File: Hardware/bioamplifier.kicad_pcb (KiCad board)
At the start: 4 copper layers, 73.2 x 45 mm, 86 parts, among them IC1 MCP1754ST-3302E_DB, J1 Conn_01x07_Socket, J2 Conn_01x26_Pin, J3 Conn_01x07_Socket, U1 ADS1299IPAG, U10 TPD4E1B06DCKR, U11 LM2665M6, U12 TLV77333PDQNR, U2 TPD4E1B06DCKR, U3 TPD4E1B06DCKR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

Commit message: Fix Last DRC Errors
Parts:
- removed IC1: MCP1754ST-3302E_DB, mcp1754:SOT230P700X180-4N
- removed U12: TLV77333PDQNR, tlv77333:X2SON_DQN4_TEX
- moved C29 31.5 mm to (118.9, 108.5), turned to -90 degrees
- moved C41 29.3 mm to (116.9, 108.5), turned to -90 degrees
- moved C25 28.7 mm to (107.8, 108.7), turned to -90 degrees
- moved C40 27.8 mm to (100.0, 107.3), turned to 90 degrees
- moved U6 26.4 mm to (116.9, 104.5), turned to 0 degrees
- moved U8 26.1 mm to (104.5, 107.5), turned to 180 degrees
- moved C46 25.8 mm to (91.0, 108.1), turned to 0 degrees
- moved C27 20.2 mm to (112.9, 102.0)
- moved C45 18.9 mm to (86.9, 109.1), turned to -90 degrees
- moved U11 18.9 mm to (86.9, 109.1), turned to 0 degrees
- moved R8 15.2 mm to (102.2, 92.0), turned to 0 degrees
- moved J3 14.2 mm to (106.0, 79.3), turned to 0 degrees
- moved R7 11.7 mm to (102.2, 89.0), turned to 0 degrees
- moved R1 11.4 mm to (100.0, 90.8), turned to -90 degrees
- moved R6 9.82 mm to (102.3, 86.9), turned to 0 degrees
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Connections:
- C11 pad 1: AVSS -> GNDA
- C12 pad 1: AVSS -> GNDA
- C13 pad 1: AVSS -> GNDA
- C14 pad 1: AVSS -> GNDA
- C15 pad 1: AVSS -> GNDA
- C16 pad 1: AVSS -> GNDA
- C17 pad 1: AVSS -> GNDA
- C18 pad 1: AVSS -> GNDA
- C2 pad 1: /DVDD -> DVDD
- C25 pad 1: AVSS -> GNDA
- C26 pad 1: AVSS -> GNDA
- C28 pad 1: AVSS -> GNDA
- C3 pad 1: /DVDD -> DVDD
- C31 pad 1: AVSS -> GNDA
- C32 pad 1: AVSS -> GNDA
- C33 pad 1: AVSS -> GNDA
- C34 pad 1: AVSS -> GNDA
- C35 pad 1: AVSS -> GNDA
- C36 pad 1: AVSS -> GNDA
- C37 pad 2: AVSS -> GNDA
- C38 pad 1: AVSS -> GNDA
- C39 pad 1: AVSS -> GNDA
- C40 pad 2: AVSS -> GNDA
- C42 pad 2: AVSS -> GNDA
- C43 pad 2: AVSS -> GNDA
- C44 pad 2: AVSS -> GNDA
- C46 pad 2: AVSS -> GNDA
- J2 pad 1: AVSS -> GNDA
- J2 pad 2: AVSS -> GNDA
- JP2 pad 2: AVSS -> GNDA
- U1 pad 31: AVSS -> GNDA
- U1 pad 50: /DVDD -> DVDD
- U1 pad 60: AVSS -> GNDA
- U10 pad 3: AVSS -> GNDA
- U11 pad 2: AVSS -> GNDA
- U2 pad 3: AVSS -> GNDA
- U3 pad 3: AVSS -> GNDA
- U4 pad 3: AVSS -> GNDA
- U5 pad 3: AVSS -> GNDA
- U7 pad 1: AVSS -> GNDA
- U8 pad 2: AVSS -> GNDA
- U8 pad 4: AVSS -> GNDA
- U9 pad 3: AVSS -> GNDA
- U9 pad 4: AVSS -> GNDA
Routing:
- net AVSS: track 43.5 -> 93.0 mm, vias 6 -> 5
- net DVDD: track 38.4 -> 79.3 mm, vias 0 -> 5
- net GNDA: track 0.00 -> 33.5 mm, vias 0 -> 9
- net /DVDD: track 23.1 -> 0.00 mm, vias 1 -> 0
- net AVDD: track 47.9 -> 68.2 mm
- net GNDD: track 31.2 -> 44.9 mm
- net (no net): track 11.4 -> 0.00 mm
- net Net-(D1-A): track 19.2 -> 9.00 mm
- net 3.3V_UNREG: track 41.0 -> 31.2 mm
- net /DOUT: track 21.9 -> 12.4 mm
- net /GPIO2: track 19.6 -> 11.8 mm
- net -2.5V_UNREG: track 4.09 -> 10.9 mm, vias 0 -> 1
- net /RESET: track 18.7 -> 12.6 mm
- net /CHIP_SEL: track 24.6 -> 18.5 mm
- net /START_CONV: track 21.8 -> 15.6 mm
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- added copper zone on In2.Cu, net DVDD
- added copper zone on B.Cu, net GNDA
- added copper zone on F.Cu, net GNDA
- added copper zone on In2.Cu, net GNDA
- removed copper zone on In2.Cu, net /DVDD
- removed copper zone on B.Cu, net AVSS
- removed copper zone on F.Cu, net AVSS
- removed copper zone on In1.Cu, net AVSS
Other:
- board size 73.2 x 45 mm -> 70 x 40 mm
- board text added: "TODO: Switch decouple caps to the back One spoke on some filter caps !"

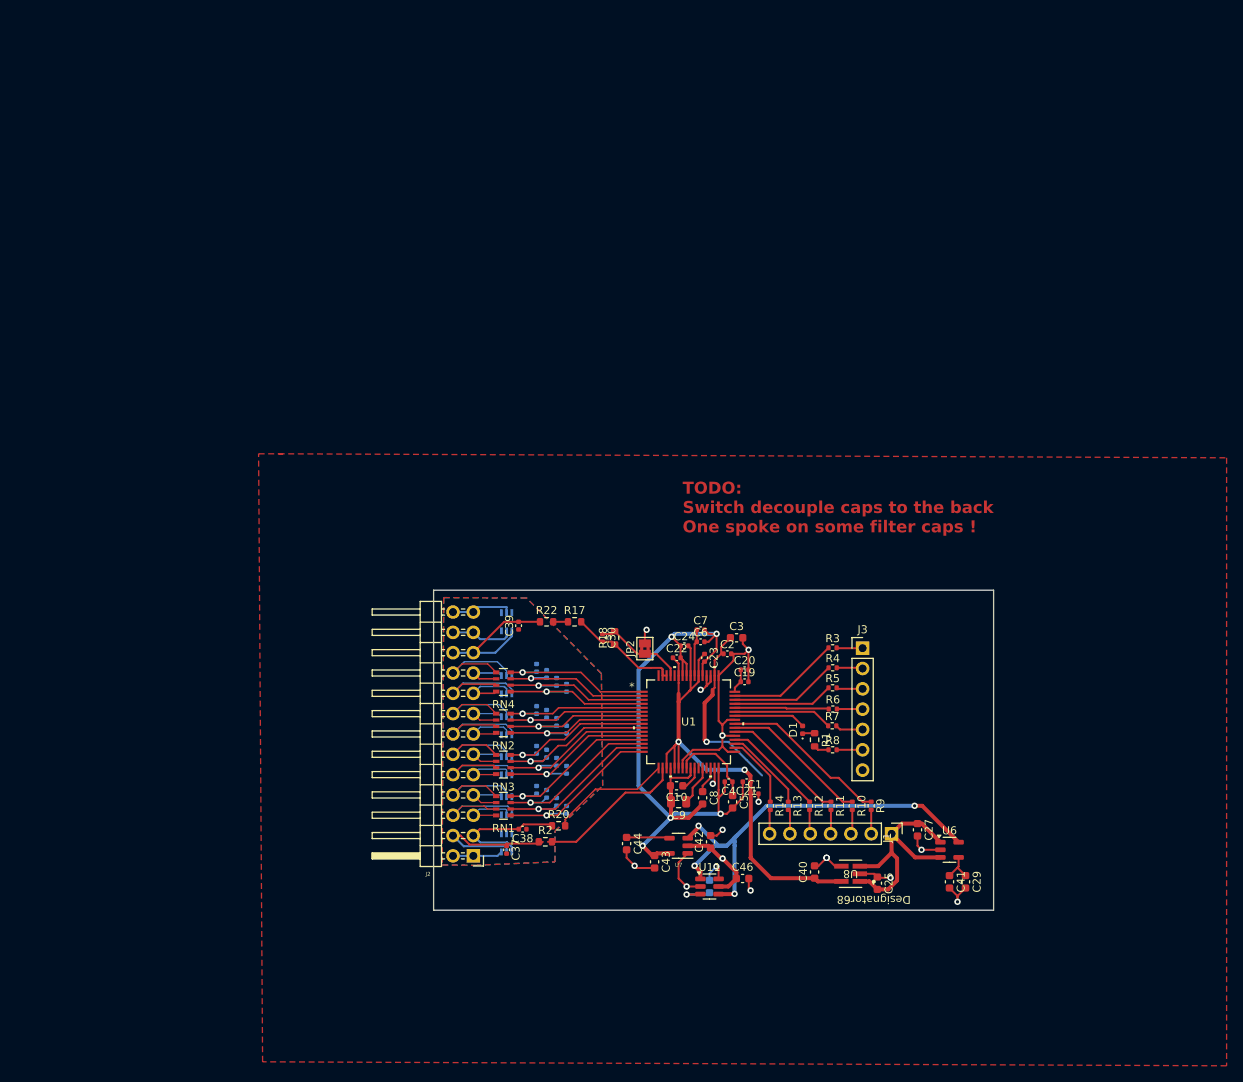
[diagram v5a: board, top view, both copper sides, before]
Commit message: Fix Label Error
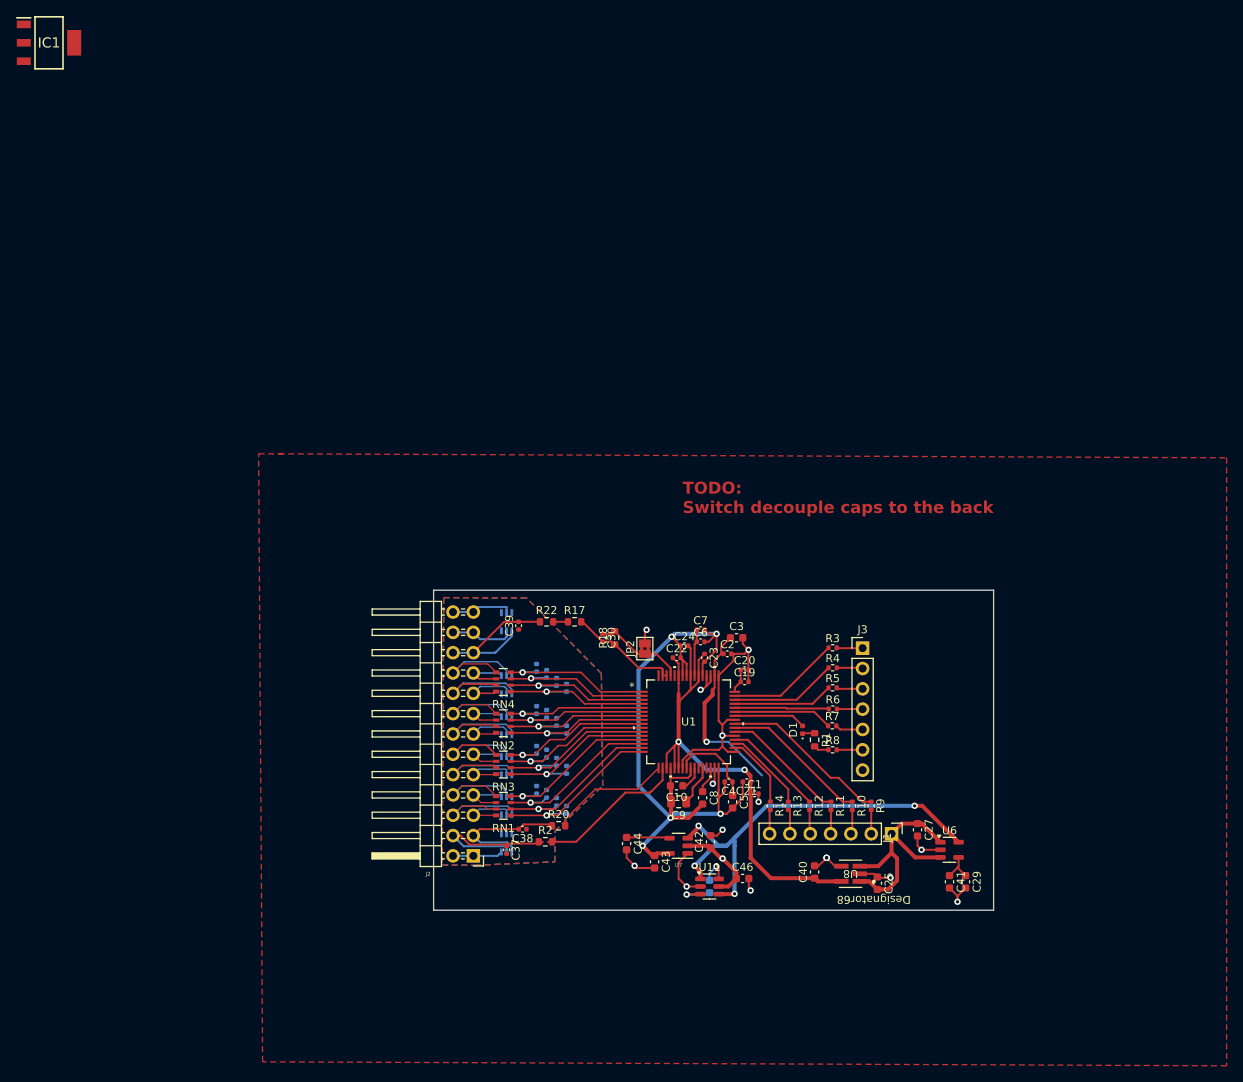
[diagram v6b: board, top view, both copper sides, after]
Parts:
- added IC1: MCP1754ST-3302E_DB, mcp1754:SOT230P700X180-4N, F.Cu at (4.30, 3.62)
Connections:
- R17 pad 1: BIASOUT -> /Electrodes input/BIASOUT_IN
- R22 pad 2: BIASOUT -> /Electrodes input/BIASOUT_IN
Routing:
- net /Electrodes input/BIASOUT_IN: track 0.00 -> 1.85 mm
- net BIASOUT: track 15.9 -> 14.3 mm
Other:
- board text added: "TODO: Switch decouple caps to the back"
- board text removed: "TODO: Switch decouple caps to the back One spoke on some filter caps !"

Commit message: Fix Grounding
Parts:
- moved R7 0.48 mm to (102.4, 89.4)
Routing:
- net /DOUT: track 12.4 -> 12.9 mm
- net GNDA: vias 9 -> 8
- removed copper zone on B.Cu, net GNDA

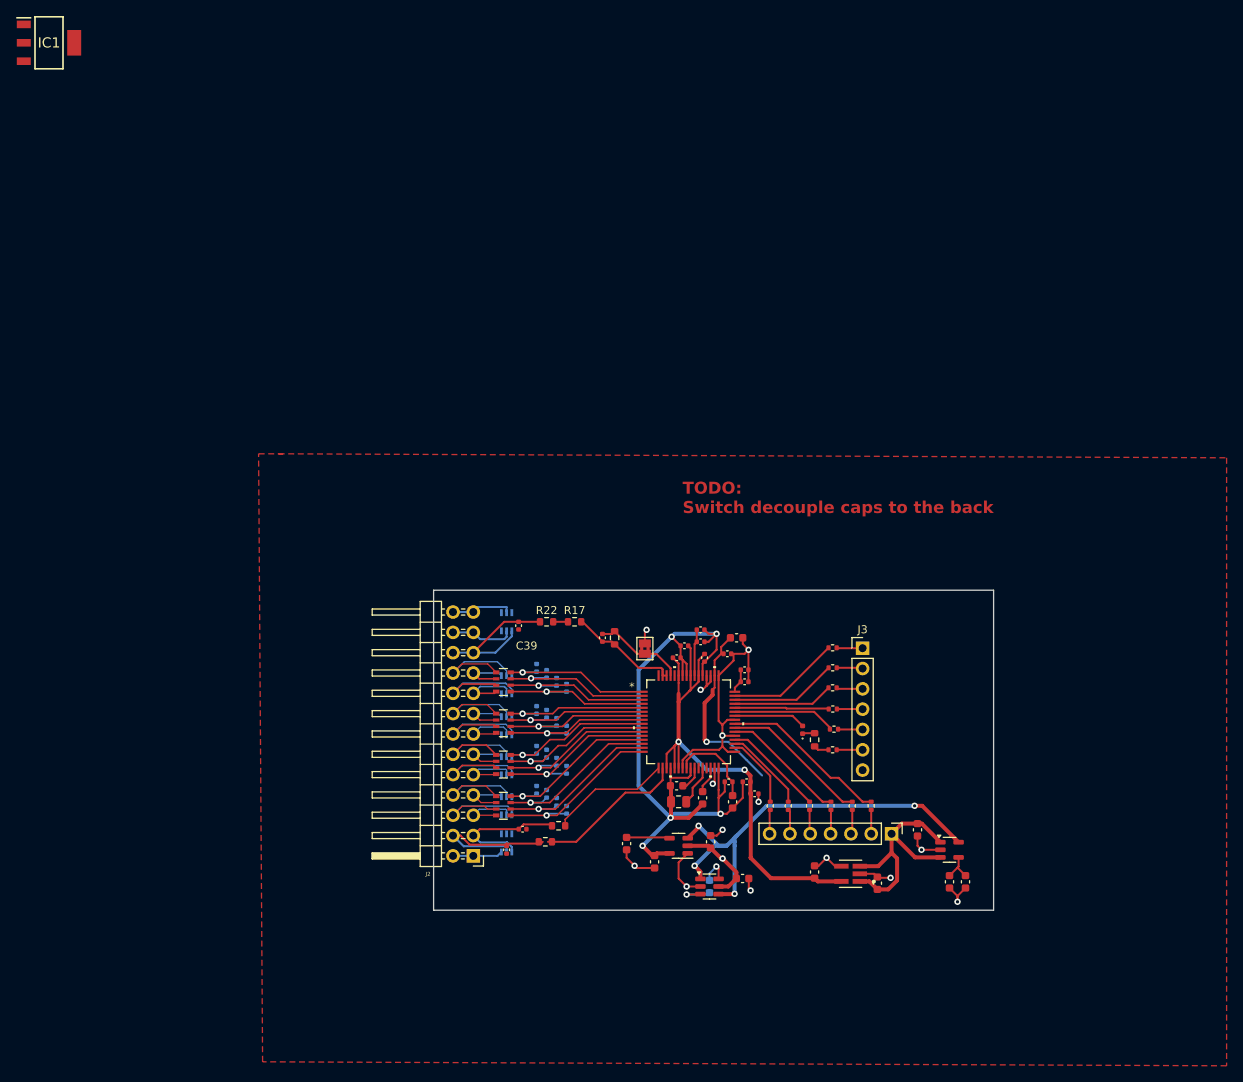
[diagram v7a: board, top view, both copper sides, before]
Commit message: Add Fiducials, Mounting holes, 3d models
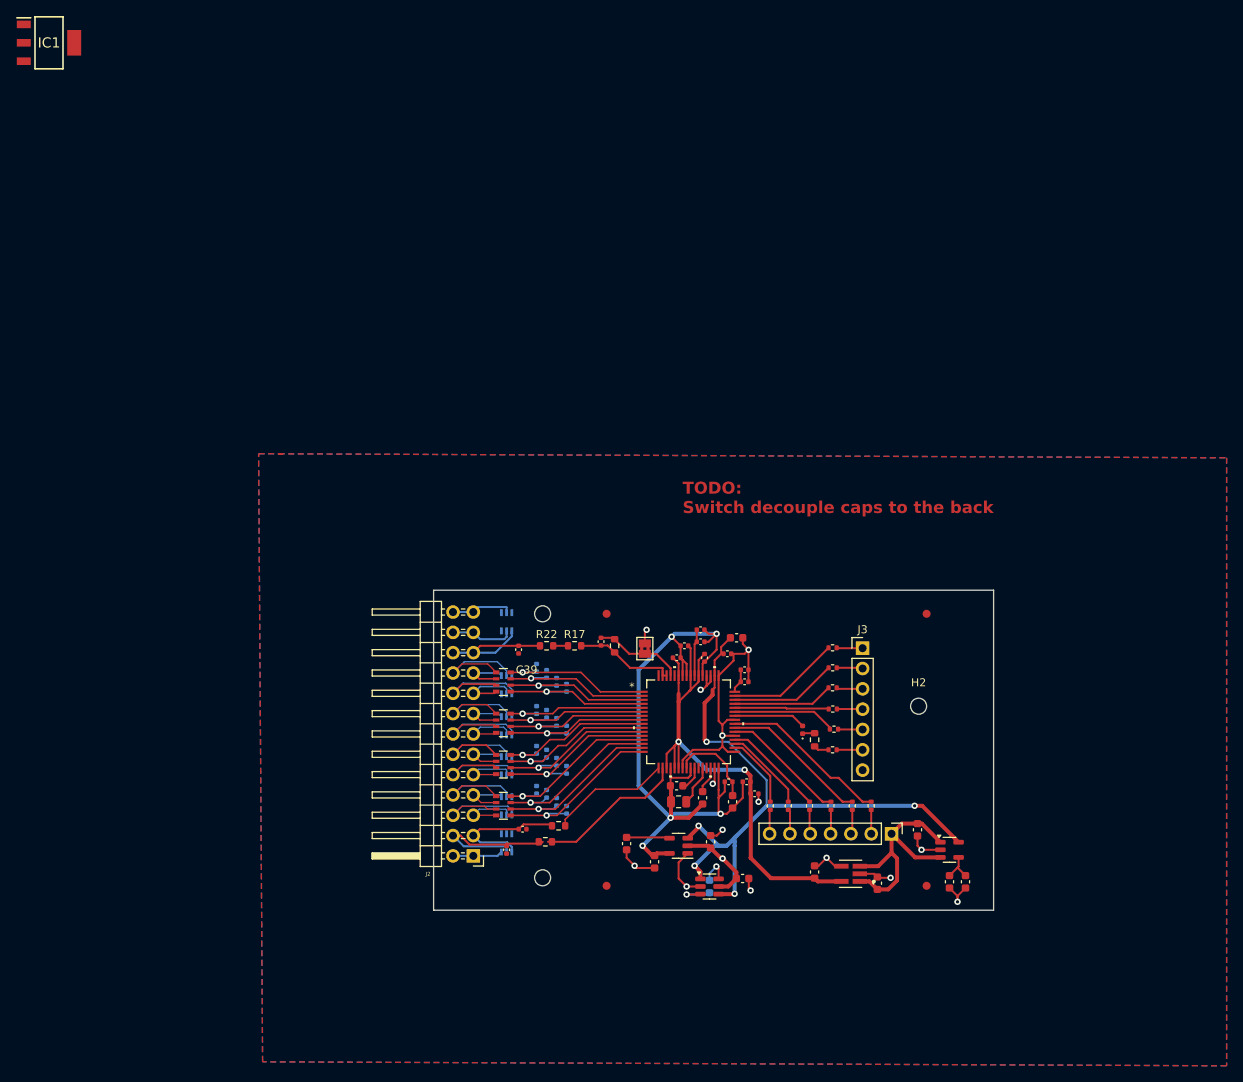
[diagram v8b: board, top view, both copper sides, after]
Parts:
- added FID1: Fiducial, Fiducial:Fiducial_1mm_Mask3mm, F.Cu at (114.0, 75.0)
- added FID2: Fiducial, Fiducial:Fiducial_1mm_Mask3mm, F.Cu at (114.0, 109.0)
- added FID3: Fiducial, Fiducial:Fiducial_1mm_Mask3mm, F.Cu at (74.0, 75.0)
- added FID4: Fiducial, Fiducial:Fiducial_1mm_Mask3mm, F.Cu at (74.0, 109.0)
- added H1: MountingHole, MountingHole:MountingHole_2mm, F.Cu at (66.0, 75.0)
- added H2: MountingHole, MountingHole:MountingHole_2mm, F.Cu at (113.0, 86.5)
- added H3: MountingHole, MountingHole:MountingHole_2mm, F.Cu at (66.0, 108.0)
- moved C39 3.00 mm to (63.0, 79.5)
- moved R17 3.00 mm to (70.0, 79.0)
- moved R22 3.00 mm to (66.5, 79.0)
- moved R18 1.00 mm to (75.0, 79.0)
- moved C30 0.51 mm to (73.3, 78.5)
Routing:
- net DVDD: track 79.3 -> 83.3 mm
- net BIASOUT: track 14.3 -> 12.8 mm
- net /Electrodes input/BIAS: track 18.8 -> 17.6 mm
- added copper zone on B.Cu, net GNDA
